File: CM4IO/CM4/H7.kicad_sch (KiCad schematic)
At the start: 65 parts

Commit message: Initial CM4IO board design
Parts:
- removed C? (x2): 1u, Capacitor_Tantalum_SMD:CP_EIA-3216-18_Kemet-A, symbol F7_100pin-rescue:CP_Small-Device
- removed C?: 2.2u, symbol Device:C_Small
- removed FB?: FCM1608KF-601T03, Inductor_SMD:L_0603_1608Metric, symbol F7_100pin-rescue:Ferrite_Bead_Small-Device
- removed FB?: 18ohm @ 100 MHz, Inductor_SMD:L_0603_1608Metric, symbol F7_100pin-rescue:Ferrite_Bead_Small-Device
- removed R? (x3): 22, symbol Device:R_Small
- added C23, C25: 1u, Capacitor_Tantalum_SMD:CP_EIA-3216-18_Kemet-A, symbol Device:C_Polarized_Small
- added FB3: 18 @100Mhz, Inductor_SMD:L_0603_1608Metric, symbol Device:FerriteBead_Small
- added L5: 39n, Inductor_SMD:L_0402_1005Metric, symbol Device:L_Small
- added R19: 10k, Resistor_SMD:R_0402_1005Metric, symbol Device:R_Small
- BT1: renamed from BT?; footprint (none) -> Battery:BatteryHolder_Keystone_3000_1x12mm
- C13: renamed from C?; footprint (none) -> Capacitor_Tantalum_SMD:CP_EIA-3216-18_Kemet-A
- C14, C15, C16, C17, C18, C19, C20, C21, C22, C27, C28, C29, C30, C31, C32, C33, C34, C35, C36, C37, C38, C44, C46, C47, C48, C49, C51, C52: renamed from C?; footprint (none) -> Capacitor_SMD:C_0402_1005Metric
- C40: renamed from C?; value 1u -> 1u_X5R_0603; footprint (none) -> Capacitor_SMD:C_0603_1608Metric
- C45: renamed from C?; footprint (none) -> Capacitor_SMD:C_0603_1608Metric
- D1: renamed from D?; footprint (none) -> Diode_SMD:D_SMA
- D2: renamed from D?; footprint (none) -> LED_SMD:LED_0603_1608Metric
- IC6: renamed from IC?; footprint QFP50P2600X2600X160-176N -> SamacSys_Parts:QFP50P2600X2600X160-176N
- L4: renamed from L?; footprint (none) -> Inductor_SMD:L_0805_2012Metric
- R20, R27: renamed from R?; footprint (none) -> Resistor_SMD:R_0402_1005Metric
- R21: renamed from R?; footprint (none) -> Resistor_SMD:R_0603_1608Metric
- SW1: renamed from SW?; footprint (none) -> Button_Switch_SMD:SW_SPDT_PCM12
- Y1: renamed from Y?; footprint (none) -> Crystal:Crystal_SMD_3225-4Pin_3.2x2.5mm
- Y2: renamed from Y?; footprint (none) -> Crystal:Crystal_SMD_3215-2Pin_3.2x1.5mm
- gave numbers to parts that had none: 15
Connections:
- net +3.3VA: now also C25.1, L5.2
- net +3.3VG: now also FB3.1, L5.1, R19.1; no longer C41.1, IC6.17 (VFBSMPS), L4.1
- net ANALOG_IN: now also IC6.36 (PC2_C); no longer IC6.21 (PF3)
- net GND: now also C23.2, C25.2
- net SWCLK: now also J3.4 (Pin_4)
- net SWDIO: now also J3.2 (Pin_2)
- net SWO: now also J3.6 (Pin_6)
- net VDDSMPS: now also C42.2, FB3.2
- net VREF+: now also C23.1
- net at IC6.174 (PDR_ON): now also R19.2
- new net VFBSMPS: C41.1, IC6.17 (VFBSMPS), L4.1
- no-connect marks 68 -> 100
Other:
- note removed: "GND NET TIE"

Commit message: Completed H7/CM4IO Board
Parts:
- removed L5: 39n, Inductor_SMD:L_0402_1005Metric, symbol Device:L_Small
- removed SW1: SW_SPDT, Button_Switch_SMD:SW_SPDT_PCM12, symbol Switch:SW_SPDT
- added FB2: 100 @ 100 MHz, Inductor_SMD:L_0603_1608Metric, symbol Device:FerriteBead_Small
- R18: value 0 -> 47
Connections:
- net +3.3VA: now also FB2.2
- net +3.3VG: now also FB2.1
- net GND: now also R27.2
- net HSE_IN: now also C49.1, Y1.1; no longer C48.2, Y1.3
- new net: C48.2, R20.2, Y1.3
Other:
- moved on the sheet: R20

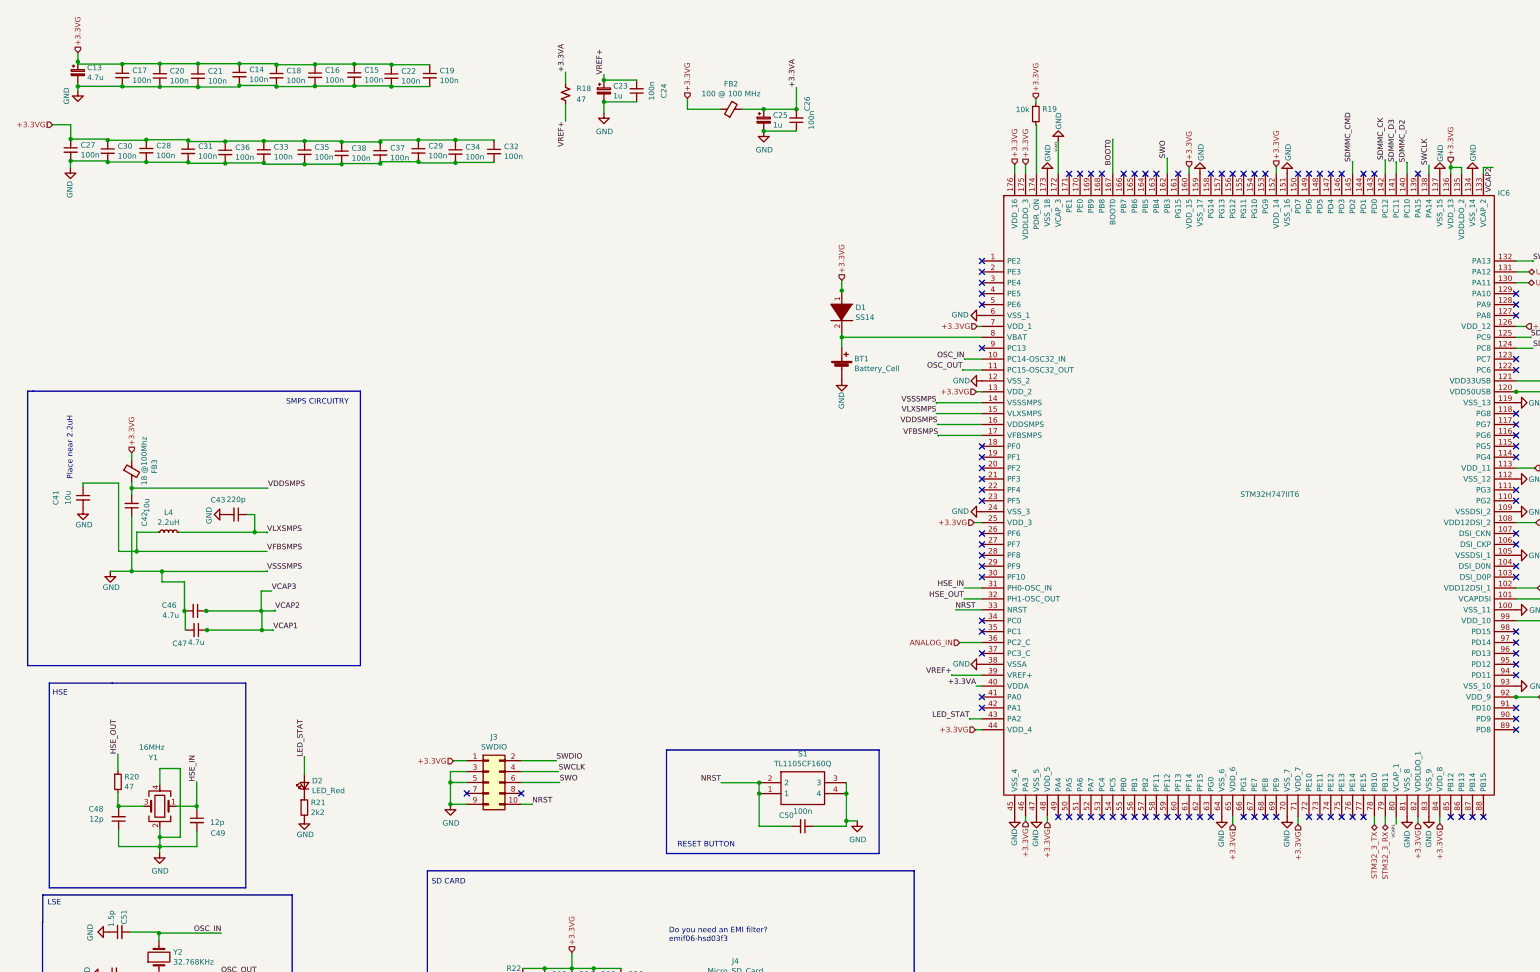
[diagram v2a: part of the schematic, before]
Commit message: Corrected SMPS configuration
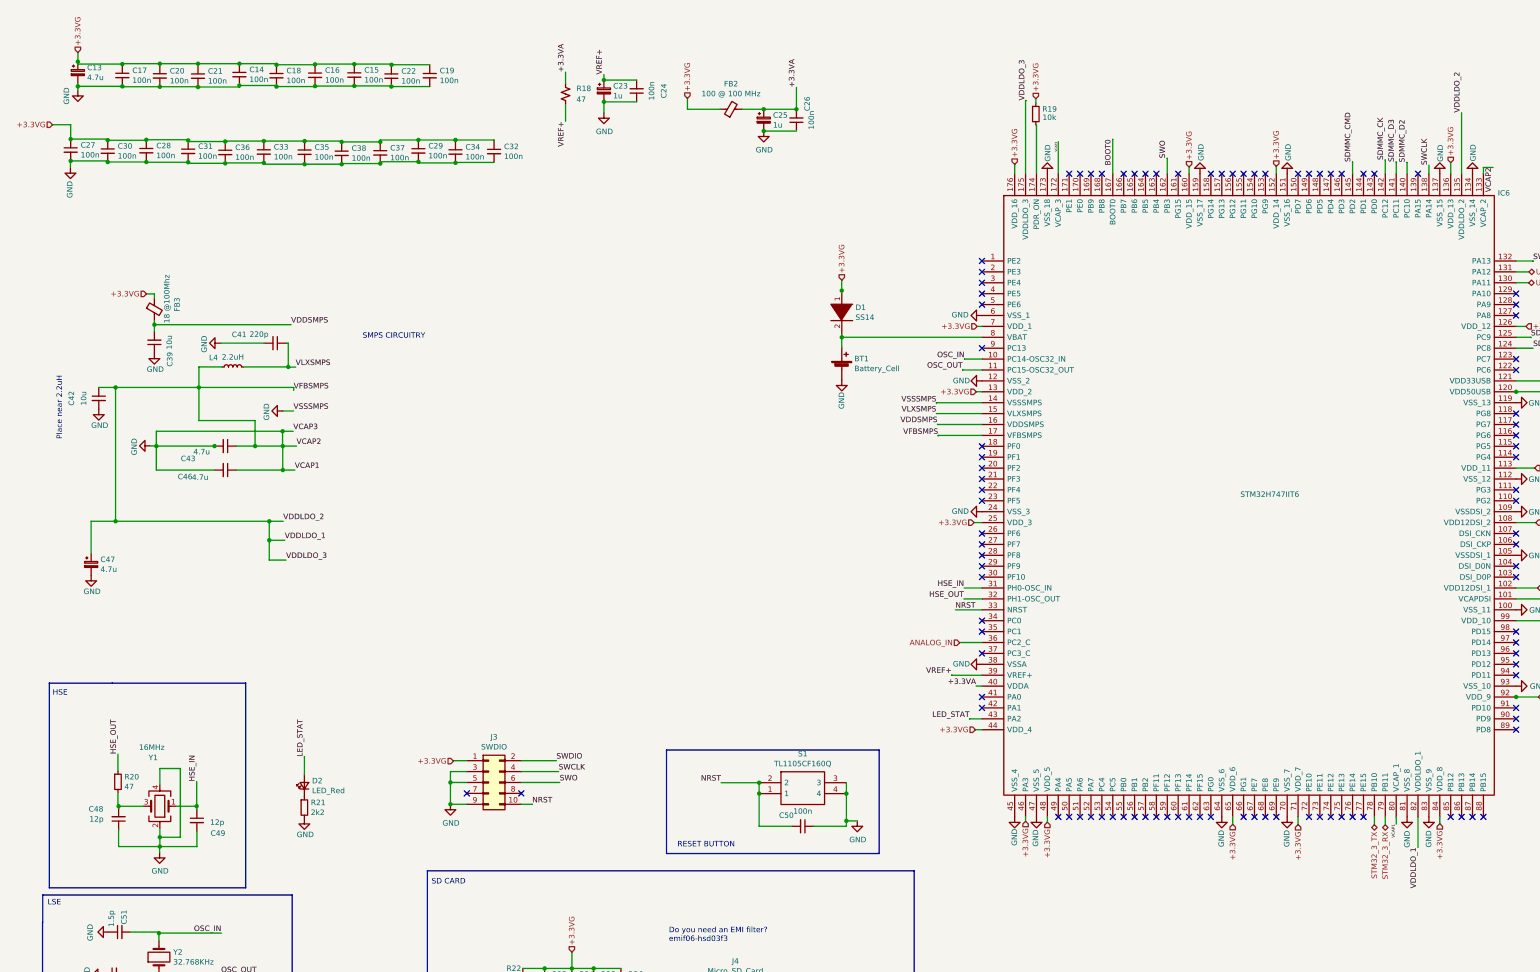
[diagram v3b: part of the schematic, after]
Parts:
- removed C47: 4.7u, Capacitor_SMD:C_0402_1005Metric, symbol Device:C_Small
- added C39: 10u, Capacitor_SMD:C_0402_1005Metric, symbol Device:C_Small
- added C47: 4.7u, Capacitor_Tantalum_SMD:CP_EIA-3216-18_Kemet-A, symbol Device:C_Polarized_Small
- C41: value 10u -> 220p
- C43: value 220p -> 4.7u
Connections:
- net +3.3VG: no longer IC6.135 (VDDLDO_2), IC6.175 (VDDLDO_3), IC6.82 (VDDLDO_1)
- net GND: now also C42.2, C39.1, C47.2; no longer C42.1, C46.1, IC6.133 (VCAP_2), IC6.80 (VCAP_1)
- net VDDSMPS: now also C39.2; no longer C42.2
- net VLXSMPS: now also C41.1; no longer C43.1
- net VFBSMPS renamed VCAP1
- net VCAP1: now also C42.1, C43.1, C46.1, IC6.133 (VCAP_2), IC6.135 (VDDLDO_2), IC6.175 (VDDLDO_3), IC6.80 (VCAP_1), IC6.82 (VDDLDO_1), C47.1; no longer C41.1
